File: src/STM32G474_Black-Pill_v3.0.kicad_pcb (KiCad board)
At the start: 2 copper layers, 100 x 100 mm, 1 part

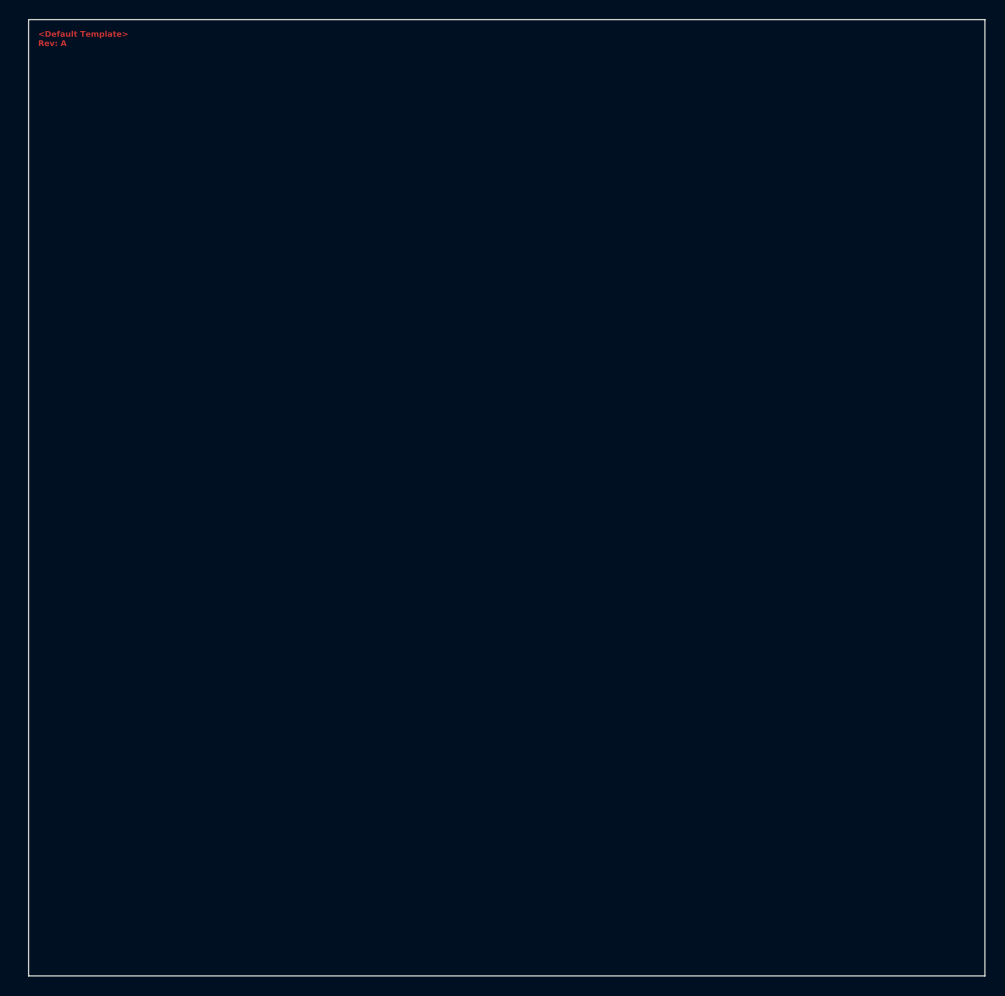
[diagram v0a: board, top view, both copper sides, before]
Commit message: Add: PCB Layout and modified schematic to suit the PCB needs
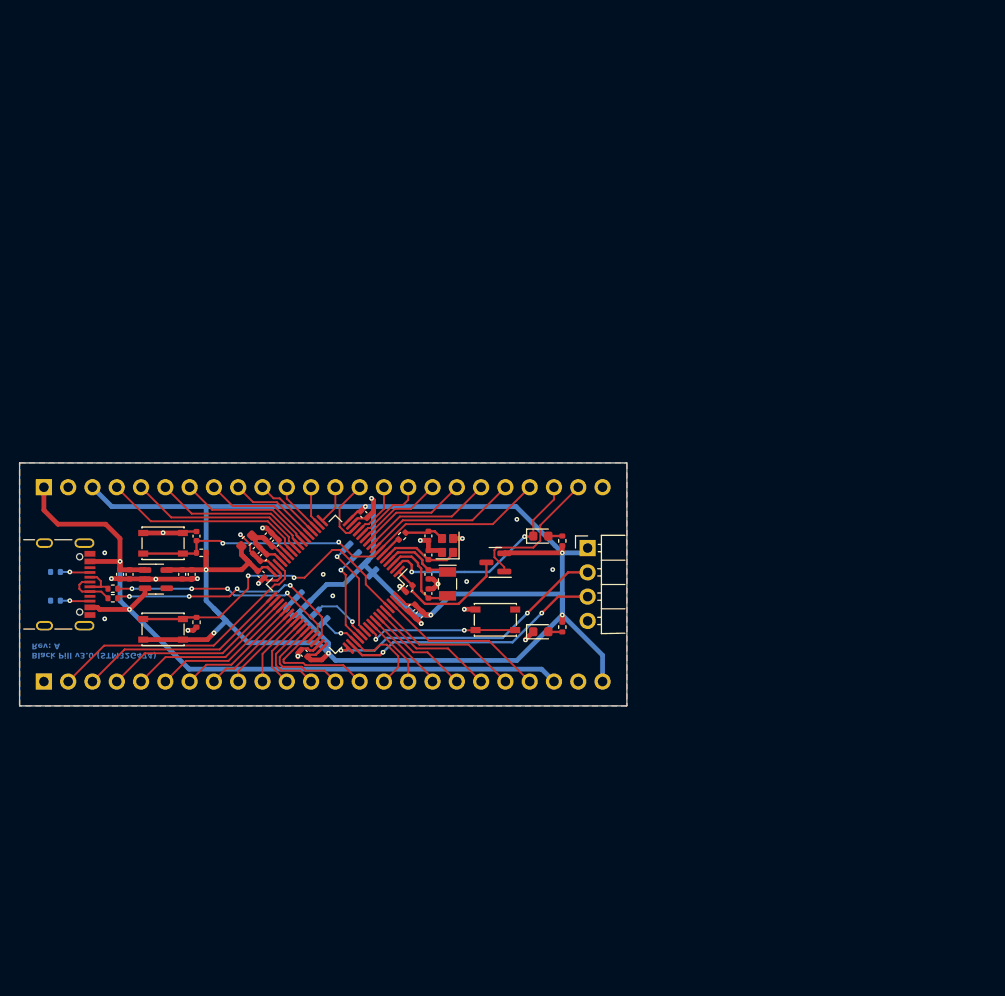
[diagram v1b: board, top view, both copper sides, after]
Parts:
- removed G0: LOGO, drawings:elektronik-emblem_3x3.5_solder
- added C101: 100nF, Capacitor_SMD:C_0402_1005Metric, B.Cu at (127.3, 102.0)
- added C102: 6pF, Capacitor_SMD:C_0402_1005Metric, F.Cu at (141.8, 96.0)
- added C103: 6pF, Capacitor_SMD:C_0402_1005Metric, F.Cu at (141.8, 94.0)
- added C104: 100nF, Capacitor_SMD:C_0402_1005Metric, F.Cu at (117.6, 94.0)
- added C105: 6pF, Capacitor_SMD:C_0402_1005Metric, F.Cu at (141.8, 100.0)
- added C106: 6pF, Capacitor_SMD:C_0402_1005Metric, F.Cu at (141.8, 98.0)
- added C107: 10µF, Capacitor_SMD:C_0402_1005Metric, F.Cu at (140.8, 102.3)
- added C108: 100nF, Capacitor_SMD:C_0402_1005Metric, F.Cu at (124.3, 98.0)
- added C109: 100nF, Capacitor_SMD:C_0402_1005Metric, F.Cu at (140.1, 101.5)
- added C110: 100nF, Capacitor_SMD:C_0402_1005Metric, F.Cu at (135.1, 91.8)
- added C111: 100nF, Capacitor_SMD:C_0402_1005Metric, F.Cu at (128.8, 106.3)
- added C112: 100nF, Capacitor_SMD:C_0402_1005Metric, F.Cu at (139.8, 99.5)
- added C113: 1µF, Capacitor_SMD:C_0402_1005Metric, F.Cu at (109.6, 98.0)
- added C114: 100nF, Capacitor_SMD:C_0402_1005Metric, F.Cu at (110.6, 98.0)
- added C115: 100nF, Capacitor_SMD:C_0402_1005Metric, F.Cu at (116.1, 98.0)
- added C116: 1µF, Capacitor_SMD:C_0402_1005Metric, F.Cu at (117.1, 98.0)
- added C117: 1µF, Capacitor_SMD:C_0402_1005Metric, F.Cu at (123.8, 95.5)
- added C118: 1µF, Capacitor_SMD:C_0402_1005Metric, F.Cu at (125.1, 94.0)
- added C119: 100nF, Capacitor_SMD:C_0402_1005Metric, F.Cu at (124.6, 96.3)
- added C120: 100nF, Capacitor_SMD:C_0402_1005Metric, F.Cu at (125.8, 94.8)
- added D101: red, LED_SMD:LED_0603_1608Metric, F.Cu at (153.6, 104.0)
- added D102: BAT54C, Package_TO_SOT_SMD:SOT-23, F.Cu at (148.8, 96.8)
- added D103: green, LED_SMD:LED_0603_1608Metric, F.Cu at (153.6, 94.0)
- added G***: LOGO, Drawings_User:elektronik-emblem_3x3.5_solder, B.Cu at (114.1, 94.8)
- added J101: USB_C_Receptacle_USB2.0, Connector_USB:USB_C_Receptacle_GCT_USB4105-xx-A_16P_TopMnt_Horizontal, F.Cu at (102.7, 99.1)
- added J102: Conn_01x20, Connector_PinHeader_2.54mm:PinHeader_1x24_P2.54mm_Vertical, B.Cu at (101.6, 109.2)
- added J103: Conn_01x20, Connector_PinHeader_2.54mm:PinHeader_1x24_P2.54mm_Vertical, B.Cu at (101.6, 88.9)
- added J104: Conn_01x04, Connector_PinHeader_2.54mm_User:PinHeader_1x04_P2.54mm_Horizontal_Board_Edge, F.Cu at (158.5, 95.3)
- added L101: 10µH, Inductor_SMD:L_0603_1608Metric, F.Cu at (122.8, 94.5)
- added R101: 5.1k, Resistor_SMD:R_0402_1005Metric, B.Cu at (102.8, 97.8)
- added R102: 5.1k, Resistor_SMD:R_0402_1005Metric, B.Cu at (102.8, 100.8)
- added R103: 10k, Resistor_SMD:R_0402_1005Metric, F.Cu at (118.1, 95.8)
- added R104: 10R, Resistor_SMD:R_0402_1005Metric, F.Cu at (108.8, 99.5)
- added R105: 10R, Resistor_SMD:R_0402_1005Metric, F.Cu at (108.8, 100.5)
- added R106: 0R, Resistor_SMD:R_0402_1005Metric, F.Cu at (139.1, 94.0)
- added R107: 100R, Resistor_SMD:R_0402_1005Metric, F.Cu at (155.8, 103.5)
- added R108: 10k, Resistor_SMD:R_0402_1005Metric, F.Cu at (117.6, 103.0)
- added R109: 100R, Resistor_SMD:R_0402_1005Metric, F.Cu at (155.8, 94.5)
- added SW101: SW_Push, Button_Switch_SMD:SW_SPST_PTS810, F.Cu at (114.1, 94.8)
- added SW102: SW_Push, Button_Switch_SMD:SW_SPST_PTS810, F.Cu at (114.1, 103.8)
- added SW103: SW_Push, Button_Switch_SMD:SW_SPST_PTS810, F.Cu at (148.8, 102.8)
- added U101: W25Q32JVSS, Package_SO:SOIC-8_5.23x5.23mm_P1.27mm, B.Cu at (132.1, 99.1)
- added U102: STM32G474RETx, Package_QFP:LQFP-64_10x10mm_P0.5mm, F.Cu at (132.1, 99.1)
- added U103: AP7343xx, Package_TO_SOT_SMD:SOT-23-5, F.Cu at (113.3, 98.5)
- added Y101: 24MHz, Crystal:Crystal_SMD_SeikoEpson_FA128-4Pin_2.0x1.6mm, F.Cu at (143.8, 95.0)
- added Y102: 32.768kHz, Crystal:Crystal_SMD_MicroCrystal_CC7V-T1A-2Pin_3.2x1.5mm, F.Cu at (143.8, 99.0)
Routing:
- net +3.3V: track 0.00 -> 218.4 mm, vias 0 -> 7
- net +5V: track 0.00 -> 81.6 mm, vias 0 -> 2
- net GND: track 0.00 -> 52.5 mm, vias 0 -> 24
- net NRST: track 0.00 -> 45.5 mm, vias 0 -> 2
- net /BOOT: track 0.00 -> 32.6 mm, vias 0 -> 2
- net /SWDIO: track 0.00 -> 30.1 mm, vias 0 -> 2
- net /PB10: track 0.00 -> 28.9 mm
- net /SWCLK: track 0.00 -> 27.7 mm, vias 0 -> 2
- net /PA12: track 0.00 -> 26.3 mm, vias 0 -> 4
- net /PA11: track 0.00 -> 24.4 mm, vias 0 -> 4
- net /PC13: track 0.00 -> 23.2 mm, vias 0 -> 2
- net /PB11: track 0.00 -> 22.4 mm
- net /PB2: track 0.00 -> 21.4 mm
- net /PB12: track 0.00 -> 20.0 mm
- net /PB1: track 0.00 -> 19.0 mm
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- added copper zone on B.Cu, net GND
- added copper zone on F.Cu, net GND
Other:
- board size 100 x 100 mm -> 63.5 x 25.4 mm
